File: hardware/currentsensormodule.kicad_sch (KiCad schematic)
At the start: 11 parts, among them J101 USART, J102 STLink, J103 Sensor1, J104 Sensor2

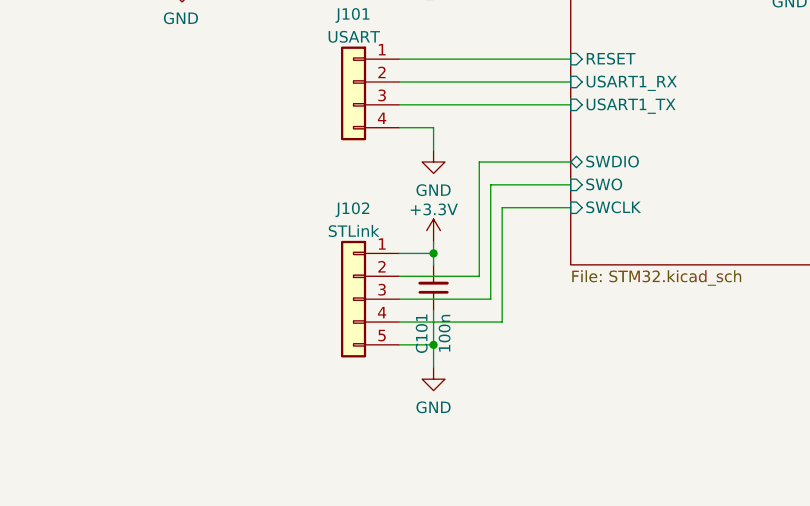
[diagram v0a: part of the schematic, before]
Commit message: STLink 3v3 protection diode, silkscreen updates
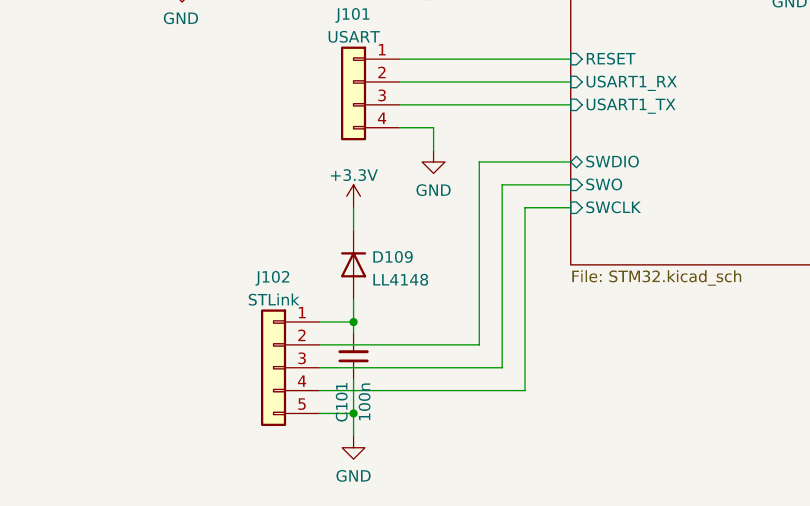
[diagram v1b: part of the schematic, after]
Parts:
- added D109: LL4148, Diode_SMD:D_MiniMELF, symbol Diode:LL4148
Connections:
- net +3V3: now also D109.1 (K); no longer C101.2, J102.1 (Pin_1)
- new net: C101.2, D109.2 (A), J102.1 (Pin_1)
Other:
- moved on the sheet: C101, J102

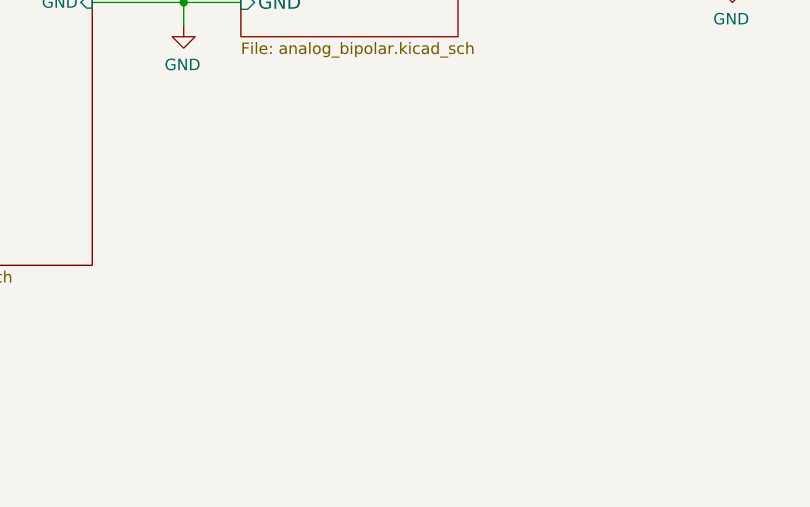
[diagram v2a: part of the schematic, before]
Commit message: hardware: fixed RJ45 footp sh pin, added shapes3D (including K78L15)
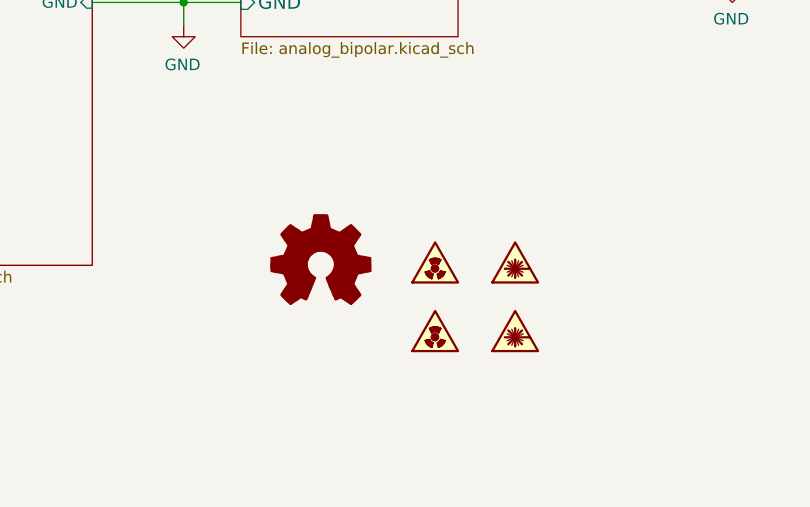
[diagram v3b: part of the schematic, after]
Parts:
- added LOGO101: Logo_Open_Hardware_Small, Symbol:OSHW-Logo2_7.3x6mm_SilkScreen, symbol Graphic:Logo_Open_Hardware_Small
- added SYM101, SYM103: SYM_Radioactive_Radiation_Small, logo:logo, symbol Graphic:SYM_Radioactive_Radiation_Small
- added SYM102, SYM104: SYM_LASER_Small, logoifsc:logoifsc, symbol Graphic:SYM_LASER_Small
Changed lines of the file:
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@@
     (pin "1")
+  )
+  (symbol (lib_id "Graphic:SYM_Radioactive_Radiation_Small") (at 207.01 142.24 0) (unit 1)
+    (in_bom no) (on_board yes) (fields_autoplaced)
+    (property "Reference" "SYM101" (id 0) (at 207.01 138.684 0)
+      (effects (font (size 1.27 1.27)) hide)
+    )
+    (property "Value" "SYM_Radioactive_Radiation_Small" (id 1) (at 207.01 145.415 0)
+      (effects (font (size 1.27 1.27)) hide)
+    )
+    (property "Footprint" "logo:logo" (id 2) (at 207.01 146.685 0)
+      (effects (font (size 1.27 1.27)) hide)
+    )
+    (property "Datasheet" "~" (id 3) (at 207.772 147.32 0)
+      (effects (font (size 1.27 1.27)) hide)
+    )
   )
   (symbol (lib_id "Diode:LL4148") (at 116.84 142.24 270) (unit 1)
@@
     (pin "1")
     (pin "2")
+  )
+  (symbol (lib_id "Graphic:SYM_Radioactive_Radiation_Small") (at 207.01 149.86 0) (unit 1)
+    (in_bom no) (on_board yes) (fields_autoplaced)
+    (property "Reference" "SYM103" (id 0) (at 207.01 146.304 0)
+      (effects (font (size 1.27 1.27)) hide)
+    )
+    (property "Value" "SYM_Radioactive_Radiation_Small" (id 1) (at 207.01 153.035 0)
+      (effects (font (size 1.27 1.27)) hide)
+    )
+    (property "Footprint" "logo:logo" (id 2) (at 207.01 154.305 0)
+      (effects (font (size 1.27 1.27)) hide)
+    )
+    (property "Datasheet" "~" (id 3) (at 207.772 154.94 0)
+      (effects (font (size 1.27 1.27)) hide)
+    )
   )
   (symbol (lib_id "Diode:LL4148") (at 62.23 66.04 180) (unit 1)
@@
     (pin "4")
   )
+  (symbol (lib_id "Graphic:SYM_LASER_Small") (at 215.9 142.24 0) (unit 1)
+    (in_bom no) (on_board yes) (fields_autoplaced)
+    (property "Reference" "SYM102" (id 0) (at 215.9 138.684 0)
+      (effects (font (size 1.27 1.27)) hide)
+    )
+    (property "Value" "SYM_LASER_Small" (id 1) (at 215.9 145.415 0)
+      (effects (font (size 1.27 1.27)) hide)
+    )
+    (property "Footprint" "logoifsc:logoifsc" (id 2) (at 215.9 146.685 0)
+      (effects (font (size 1.27 1.27)) hide)
+    )
+    (property "Datasheet" "~" (id 3) (at 216.662 147.32 0)
+      (effects (font (size 1.27 1.27)) hide)
+    )
+  )
   (symbol (lib_id "Connector_Generic:Conn_01x05") (at 107.95 153.67 0) (mirror y) (unit 1)
     (in_bom yes) (on_board yes) (fields_autoplaced)
@@
     (pin "5")
   )
+  (symbol (lib_id "Graphic:SYM_LASER_Small") (at 215.9 149.86 0) (unit 1)
+    (in_bom no) (on_board yes) (fields_autoplaced)
+    (property "Reference" "SYM104" (id 0) (at 215.9 146.304 0)
+      (effects (font (size 1.27 1.27)) hide)
+    )
+    (property "Value" "SYM_LASER_Small" (id 1) (at 215.9 153.035 0)
+      (effects (font (size 1.27 1.27)) hide)
+    )
+    (property "Footprint" "logoifsc:logoifsc" (id 2) (at 215.9 154.305 0)
+      (effects (font (size 1.27 1.27)) hide)
+    )
+    (property "Datasheet" "~" (id 3) (at 216.662 154.94 0)
+      (effects (font (size 1.27 1.27)) hide)
+    )
+  )
   (symbol (lib_id "Device:Fuse") (at 50.8 66.04 90) (unit 1)
     (in_bom yes) (on_board yes) (fields_autoplaced)
@@
     (pin "1")
     (pin "2")
+  )
+  (symbol (lib_id "Graphic:Logo_Open_Hardware_Small") (at 194.31 142.24 0) (unit 1)
+    (in_bom no) (on_board yes) (fields_autoplaced)
+    (property "Reference" "LOGO101" (id 0) (at 194.31 135.255 0)
+      (effects (font (size 1.27 1.27)) hide)
+    )
+    (property "Value" "Logo_Open_Hardware_Small" (id 1) (at 194.31 147.955 0)
+      (effects (font (size 1.27 1.27)) hide)
+    )
+    (property "Footprint" "Symbol:OSHW-Logo2_7.3x6mm_SilkScreen" (id 2) (at 194.31 142.24 0)
+      (effects (font (size 1.27 1.27)) hide)
+    )
+    (property "Datasheet" "~" (id 3) (at 194.31 142.24 0)
+      (effects (font (size 1.27 1.27)) hide)
+    )
   )
   (sheet (at 185.42 95.25) (size 24.13 21.59) (fields_autoplaced)
@@
       (reference "J106") (unit 1) (value "RJ45") (footprint "KicadZeniteSolarLibrary18:RJ45_YH59_01")
     )
+    (path "/fc2a1509-ad5f-416f-96c7-14370948709b"
+      (reference "LOGO101") (unit 1) (value "Logo_Open_Hardware_Small") (footprint "Symbol:OSHW-Logo2_7.3x6mm_SilkScreen")
+    )
     (path "/00000000-0000-0000-0000-000062102577/00000000-0000-0000-0000-00005aab5ef4"
       (reference "R101") (unit 1) (value "30") (footprint "Resistor_SMD:R_0603_1608Metric_Pad0.98x0.95mm_HandSolder")
@@
       (reference "R302") (unit 1) (value "10k") (footprint "Resistor_SMD:R_0603_1608Metric_Pad0.98x0.95mm_HandSolder")
     )
+    (path "/66db944e-15d2-4c8d-8dcc-ffa5424e7299"
+      (reference "SYM101") (unit 1) (value "SYM_Radioactive_Radiation_Small") (footprint "logo:logo")
+    )
+    (path "/a8c8fe94-7e9f-456b-ab0b-42ed75fa4df2"
+      (reference "SYM102") (unit 1) (value "SYM_LASER_Small") (footprint "logoifsc:logoifsc")
+    )
+    (path "/76b36edb-8986-48d4-832f-1ae513cc4d71"
+      (reference "SYM103") (unit 1) (value "SYM_Radioactive_Radiation_Small") (footprint "logo:logo")
+    )
+    (path "/b981c534-dd1a-4eb2-890f-b8d4fccae19c"
+      (reference "SYM104") (unit 1) (value "SYM_LASER_Small") (footprint "logoifsc:logoifsc")
+    )
     (path "/00000000-0000-0000-0000-000062102577/00000000-0000-0000-0000-00005aab7477"

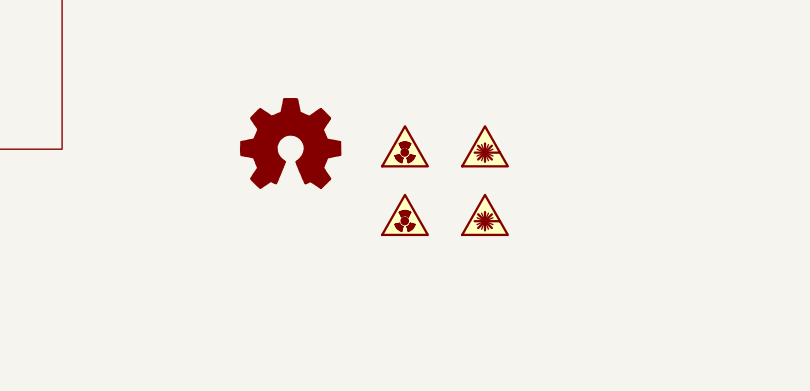
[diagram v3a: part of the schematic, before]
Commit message: Pequenas mudanças na silkscreen
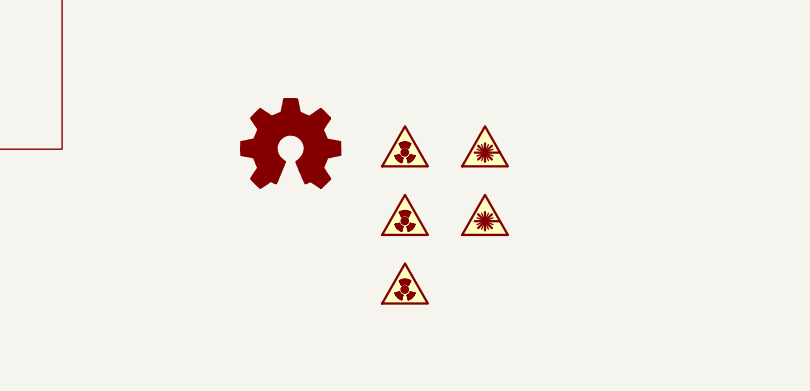
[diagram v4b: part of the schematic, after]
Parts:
- added SYM105: (no value), symbol Graphic:SYM_Radioactive_Radiation_Small
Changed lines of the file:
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@@
     (pin "2")
+  )
+  (symbol (lib_id "Graphic:SYM_Radioactive_Radiation_Small") (at 207.01 157.48 0) (unit 1)
+    (in_bom no) (on_board yes) (fields_autoplaced)
+    (property "Reference" "SYM105" (id 0) (at 207.01 153.924 0)
+      (effects (font (size 1.27 1.27)) hide)
+    )
+    (property "Value" "" (id 1) (at 207.01 160.655 0)
+      (effects (font (size 1.27 1.27)) hide)
+    )
+    (property "Footprint" "" (id 2) (at 207.01 161.925 0)
+      (effects (font (size 1.27 1.27)) hide)
+    )
+    (property "Datasheet" "~" (id 3) (at 207.772 162.56 0)
+      (effects (font (size 1.27 1.27)) hide)
+    )
   )
   (symbol (lib_id "power:+3.3V") (at 116.84 135.89 0) (unit 1)
@@
       (reference "SYM104") (unit 1) (value "SYM_LASER_Small") (footprint "logoifsc:logoifsc")
     )
+    (path "/d1dcc432-f13b-4b72-b3ad-1fe8f8ed0869"
+      (reference "SYM105") (unit 1) (value "SYM_Radioactive_Radiation_Small") (footprint "naolavar:naolavar")
+    )
     (path "/00000000-0000-0000-0000-000062102577/00000000-0000-0000-0000-00005aab7477"

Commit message: hardware: Silkscreen ajusted, RDC errors fixed
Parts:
- SYM101, SYM103: value SYM_Radioactive_Radiation_Small -> (none); footprint logo:logo -> (none)
- SYM102, SYM104: value SYM_LASER_Small -> (none); footprint logoifsc:logoifsc -> (none)
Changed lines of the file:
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@@
       (effects (font (size 1.27 1.27)) hide)
     )
-    (property "Value" "SYM_Radioactive_Radiation_Small" (id 1) (at 207.01 145.415 0)
-      (effects (font (size 1.27 1.27)) hide)
-    )
-    (property "Footprint" "logo:logo" (id 2) (at 207.01 146.685 0)
+    (property "Value" "" (id 1) (at 207.01 145.415 0)
+      (effects (font (size 1.27 1.27)) hide)
+    )
+    (property "Footprint" "" (id 2) (at 207.01 146.685 0)
       (effects (font (size 1.27 1.27)) hide)
     )
@@
       (effects (font (size 1.27 1.27)) hide)
     )
-    (property "Value" "SYM_Radioactive_Radiation_Small" (id 1) (at 207.01 153.035 0)
-      (effects (font (size 1.27 1.27)) hide)
-    )
-    (property "Footprint" "logo:logo" (id 2) (at 207.01 154.305 0)
+    (property "Value" "" (id 1) (at 207.01 153.035 0)
+      (effects (font (size 1.27 1.27)) hide)
+    )
+    (property "Footprint" "" (id 2) (at 207.01 154.305 0)
       (effects (font (size 1.27 1.27)) hide)
     )
@@
       (effects (font (size 1.27 1.27)) hide)
     )
-    (property "Value" "SYM_LASER_Small" (id 1) (at 215.9 145.415 0)
-      (effects (font (size 1.27 1.27)) hide)
-    )
-    (property "Footprint" "logoifsc:logoifsc" (id 2) (at 215.9 146.685 0)
+    (property "Value" "" (id 1) (at 215.9 145.415 0)
+      (effects (font (size 1.27 1.27)) hide)
+    )
+    (property "Footprint" "" (id 2) (at 215.9 146.685 0)
       (effects (font (size 1.27 1.27)) hide)
     )
@@
       (effects (font (size 1.27 1.27)) hide)
     )
-    (property "Value" "SYM_LASER_Small" (id 1) (at 215.9 153.035 0)
-      (effects (font (size 1.27 1.27)) hide)
-    )
-    (property "Footprint" "logoifsc:logoifsc" (id 2) (at 215.9 154.305 0)
+    (property "Value" "" (id 1) (at 215.9 153.035 0)
+      (effects (font (size 1.27 1.27)) hide)
+    )
+    (property "Footprint" "" (id 2) (at 215.9 154.305 0)
       (effects (font (size 1.27 1.27)) hide)
     )
@@
     )
     (path "/66db944e-15d2-4c8d-8dcc-ffa5424e7299"
-      (reference "SYM101") (unit 1) (value "SYM_Radioactive_Radiation_Small") (footprint "logo:logo")
+      (reference "SYM101") (unit 1) (value "SYM_Radioactive_Radiation_Small") (footprint "KicadZeniteSolarLibrary18:symbol_logoZenite")
     )
     (path "/a8c8fe94-7e9f-456b-ab0b-42ed75fa4df2"
-      (reference "SYM102") (unit 1) (value "SYM_LASER_Small") (footprint "logoifsc:logoifsc")
+      (reference "SYM102") (unit 1) (value "SYM_LASER_Small") (footprint "KicadZeniteSolarLibrary18:synbol_logoifsc")
     )
     (path "/76b36edb-8986-48d4-832f-1ae513cc4d71"
-      (reference "SYM103") (unit 1) (value "SYM_Radioactive_Radiation_Small") (footprint "logo:logo")
+      (reference "SYM103") (unit 1) (value "SYM_Radioactive_Radiation_Small") (footprint "KicadZeniteSolarLibrary18:symbol_logoZenite")
     )
     (path "/b981c534-dd1a-4eb2-890f-b8d4fccae19c"
-      (reference "SYM104") (unit 1) (value "SYM_LASER_Small") (footprint "logoifsc:logoifsc")
+      (reference "SYM104") (unit 1) (value "SYM_LASER_Small") (footprint "KicadZeniteSolarLibrary18:synbol_logoifsc")
     )
     (path "/d1dcc432-f13b-4b72-b3ad-1fe8f8ed0869"
-      (reference "SYM105") (unit 1) (value "SYM_Radioactive_Radiation_Small") (footprint "naolavar:naolavar")
+      (reference "SYM105") (unit 1) (value "SYM_Radioactive_Radiation_Small") (footprint "KicadZeniteSolarLibrary18:symbol_naolavar")
     )
     (path "/00000000-0000-0000-0000-000062102577/00000000-0000-0000-0000-00005aab7477"
